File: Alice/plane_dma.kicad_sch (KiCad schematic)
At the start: 108 parts, among them Q647 NOT_OC, Q648 NOT_OC, Q649 NOT_OC, Q650 NOT_OC, Q651 NOT_OC, Q652 NOT_OC, Q653 NOT_OC, Q654 NOT_OC, Q655 NOT_OC, Q656 NOT_OC, Q657 NOT_OC, Q658 NOT_OC, Q659 NOT_OC, Q660 NOT_OC, Q661 NOT_OC, Q662 NOT_OC, Q663 NOT_OC, Q664 NOT_OC, Q665 NOT_OC, Q666 NOT_OC, Q667 NOT_OC, Q668 NOT_OC, Q669 NOT_OC, Q670 NOT_OC, Q671 NOT_OC, Q672 NOT_OC, Q673 NOT_OC, Q674 NOT_OC, Q675 NOT_OC, Q676 NOT_OC

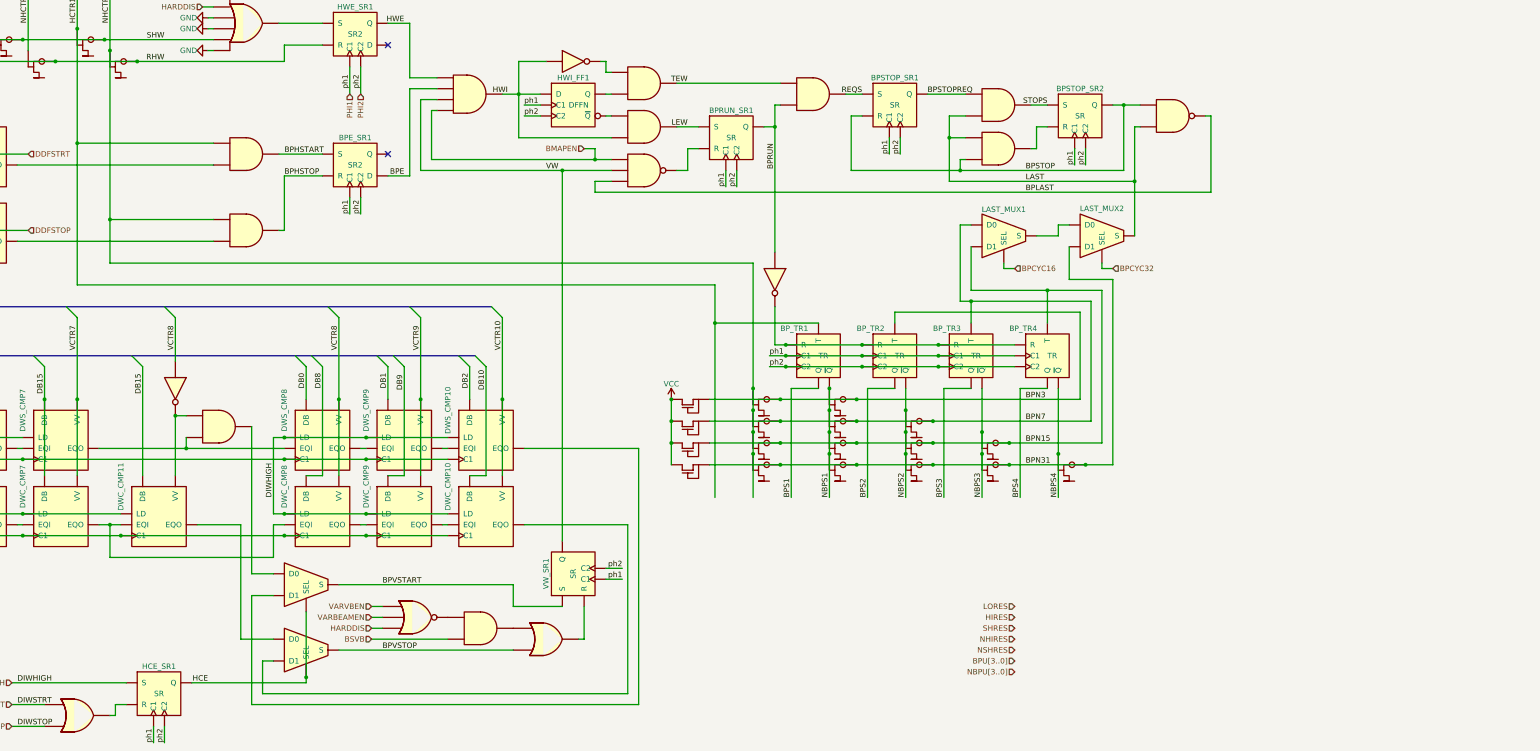
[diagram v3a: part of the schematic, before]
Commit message: Bitplane modulo logic added
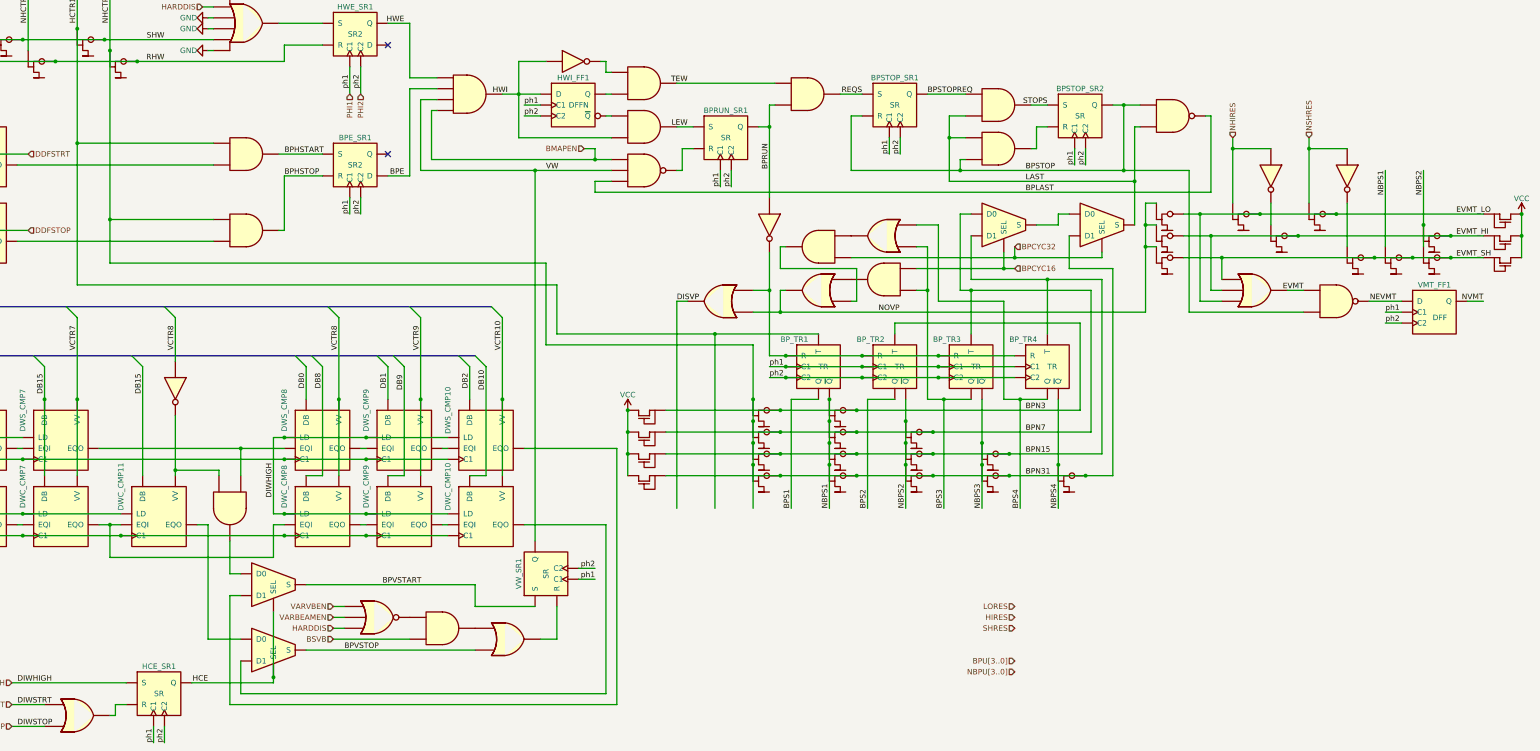
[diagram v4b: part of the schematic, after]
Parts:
- added AND_107, AND_108: AND2, symbol NMOS:AND2
- added NAND_8: NAND2, symbol NMOS:NAND2
- added NOT_33, NOT_34: NOT, symbol NMOS:NOT
- added OR_33, OR_34, OR_35: OR2, symbol NMOS:OR2
- added OR_36: OR3, symbol NMOS:OR3
- added Q685, Q686, Q687, Q688, Q689, Q690, Q691, Q692, Q693, Q694: NOT_OC, symbol NMOS:NOT_OC
- added R85, R86, R87: PULLUP, symbol NMOS:PULLUP
- added VMT_FF1: DFF, symbol NMOS:DFF
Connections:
- net BPCYC16: now also AND_108.3
- net BPCYC32: now also AND_107.2
- net BPS3: now also AND_108.2, OR_35.2
- net BPS4: now also OR_35.3
- net BPSTOP: now also NAND_8.3
- net NBPS1: now also Q692.2
- net NBPS2: now also Q693.2, Q694.2
- net NHIRES: now also NOT_33.2, Q688.2
- net NSHRES: now also NOT_34.2, Q690.2
- net PHI1: now also VMT_FF1.4 (C1)
- net PHI2: now also VMT_FF1.5 (C2)
- net VCC: now also R85.1 (S), R86.1 (S), R87.1 (S)
- net at BP_TR1.3 (R), BP_TR2.3 (R), BP_TR3.3 (R)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: now also OR_33.3
- net at DWC_CMP11.2 (VV), NOT_31.1: now also AND_94.3; no longer AND_94.2
- net at DWS_CMP7.6 (EQO), DWS_CMP8.5 (EQI): now also AND_94.2; no longer AND_94.3
- new net: NOT_34.1, Q691.2
- new net: NOT_33.1, Q689.2
- new net: AND_107.1, OR_34.2
- new net: AND_108.1, OR_34.3
- new net: AND_107.3, OR_35.1
- new net DISVP: OR_33.1
- new net EVMT: NAND_8.2, OR_36.1
- new net EVMT_HI: OR_36.3, Q686.1, Q689.1, Q693.1, R86.3 (D)
- new net EVMT_LO: OR_36.2, Q685.1, Q688.1, Q690.1, R85.3 (D)
- new net EVMT_SH: OR_36.4, Q687.1, Q691.1, Q692.1, Q694.1, R87.3 (D)
- new net NEVMT: NAND_8.1, VMT_FF1.3 (D)
- new net NOVP: OR_33.2, OR_34.1, Q685.2, Q686.2, Q687.2
- new net NVMT: VMT_FF1.1 (Q)
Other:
- moved on the sheet: BPRUN_SR1, BP_TR1, BP_TR2, BP_TR3, BP_TR4, VW_SR1

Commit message: Bitplane DMA runs in simulation
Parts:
- added AND_109: AND3, symbol NMOS:AND3
- added AND_110, AND_111, AND_112, AND_113, AND_114, AND_115, AND_116, AND_117, AND_118, AND_119, AND_120, AND_121, AND_122, AND_123, AND_124, AND_125, AND_126, AND_127: AND2, symbol NMOS:AND2
- added NOR_32, NOR_33: NOR2, symbol NMOS:NOR2
- added NOT_35: NOT, symbol NMOS:NOT
- added OR_37, OR_38, OR_39: OR6, symbol NMOS:OR6
- added OR_40: OR3, symbol NMOS:OR3
- added OR_41, OR_42, OR_43: OR2, symbol NMOS:OR2
- added Q695, Q696, Q697, Q698, Q699, Q700, Q701, Q702, Q703, Q704, Q705, Q706, Q707, Q708, Q709, Q710, Q711, Q712, Q713, Q714, Q715, Q716, Q717, Q718, Q719, Q720, Q721, Q722, Q723, Q724, Q725, Q726, Q727, Q728, Q729, Q730, Q731, Q732, Q733, Q734, Q735, Q736, Q737, Q738, Q739, Q740, Q741, Q742, Q743, Q744, Q745, Q746, Q747, Q748, Q749, Q750, Q751, Q752, Q753, Q754, Q755, Q756, Q757, Q758, Q759, Q760, Q761, Q762, Q763, Q764, Q765, Q766, Q767, Q768, Q769, Q770, Q771, Q772, Q773, Q774, Q775, Q776, Q777, Q778, Q779, Q780, Q781, Q782, Q783, Q784, Q785, Q786, Q787, Q788, Q789, Q790, Q791, Q792, Q793, Q794, Q795, Q796, Q797, Q798, Q799, Q800, Q801, Q802, Q803, Q804, Q805, Q806, Q807, Q808, Q809, Q810, Q811, Q812, Q813, Q814, Q815, Q816, Q817, Q818, Q819, Q820, Q821, Q822, Q823, Q824, Q825, Q826, Q827, Q828, Q829, Q830, Q831, Q832, Q833, Q834, Q835, Q836, Q837, Q838, Q839, Q840, Q841, Q842, Q843, Q844, Q845, Q846, Q847, Q848, Q849, Q850, Q851, Q852, Q853, Q854, Q855, Q856, Q857, Q858, Q859, Q860, Q861, Q862, Q863, Q864, Q865, Q866, Q867, Q868, Q869, Q870, Q871, Q872, Q873, Q874, Q875, Q876, Q877, Q878, Q879, Q880, Q881, Q882, Q883, Q884, Q885, Q886, Q887, Q888, Q889, Q890, Q891, Q892, Q893, Q894, Q895, Q896, Q897: NOT_OC, symbol NMOS:NOT_OC
- added R100, R101, R102, R103, R104, R105, R106, R107, R108, R88, R89, R90, R91, R92, R93, R94, R95, R96, R97, R98, R99: PULLUP, symbol NMOS:PULLUP
- added UVP_FF1, UVP_FF2, UVP_FF3, UVP_FF4, UVP_FF5, UVP_FF6, UVP_FF7, UVP_FF8: DFF, symbol NMOS:DFF
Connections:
- net BPS1: now also AND_114.2, AND_118.2, Q730.2, Q731.2, Q732.2, Q733.2, Q734.2, Q735.2
- net BPS2: now also AND_112.2, AND_119.2, AND_120.2, AND_124.2, AND_126.2, Q744.2, Q745.2
- net DISVP: now also Q695.2, Q696.2, Q697.2, Q698.2, Q699.2, Q700.2, Q701.2, Q702.2, Q703.2, Q704.2, Q705.2, Q706.2, Q707.2, Q708.2, Q709.2, Q710.2, Q711.2, Q712.2
- net GND: now also OR_38.5, OR_39.4
- net HCTR1: now also AND_113.2, Q713.2, Q714.2, Q715.2, Q716.2, Q717.2, Q718.2, Q719.2
- net NBPS1: now also AND_117.2, AND_121.2, Q736.2, Q737.2, Q738.2, Q739.2, Q740.2, Q741.2, Q742.2, Q743.2
- net NBPS2: now also AND_115.2, AND_122.2, AND_123.2, AND_125.2, AND_127.2, Q746.2, Q747.2, Q748.2, Q749.2
- net NHCTR1: now also AND_116.2, Q720.2, Q721.2, Q722.2, Q723.2, Q724.2, Q725.2, Q726.2, Q727.2, Q728.2, Q729.2
- net NHIRES: now also Q808.2, Q809.2, Q810.2, Q811.2, Q812.2, Q813.2, Q814.2, Q815.2, Q816.2, Q817.2, Q818.2, Q819.2, Q820.2, Q821.2, Q822.2, Q823.2
- net NSHRES: now also Q826.2, Q827.2, Q828.2, Q829.2, Q830.2, Q831.2, Q832.2, Q833.2, Q834.2, Q835.2, Q836.2
- net NVMT: now also NOR_32.3, NOR_33.2
- net PHI1: now also UVP_FF1.4 (C1), UVP_FF2.4 (C1), UVP_FF3.4 (C1), UVP_FF4.4 (C1), UVP_FF5.4 (C1), UVP_FF6.4 (C1), UVP_FF7.4 (C1), UVP_FF8.4 (C1)
- net PHI2: now also UVP_FF1.5 (C2), UVP_FF2.5 (C2), UVP_FF3.5 (C2), UVP_FF4.5 (C2), UVP_FF5.5 (C2), UVP_FF6.5 (C2), UVP_FF7.5 (C2), UVP_FF8.5 (C2)
- net VCC: now also R100.1 (S), R101.1 (S), R102.1 (S), R103.1 (S), R104.1 (S), R105.1 (S), R106.1 (S), R107.1 (S), R108.1 (S), R88.1 (S), R89.1 (S), R90.1 (S), R91.1 (S), R92.1 (S), R93.1 (S), R94.1 (S), R95.1 (S), R96.1 (S), R97.1 (S), R98.1 (S), R99.1 (S)
- net at NOT_34.1, Q691.2: now also Q837.2, Q838.2, Q839.2, Q840.2, Q841.2
- net at NOT_33.1, Q689.2: now also Q824.2, Q825.2
- new net: AND_125.1, OR_42.3
- new net: AND_117.1, OR_38.4
- new net: AND_122.1, OR_40.3
- new net: AND_114.1, OR_37.7
- new net: AND_124.1, OR_41.3
- new net: AND_126.1, OR_43.3
- new net: AND_115.1, OR_38.2
- new net: AND_119.1, OR_39.6
- new net: AND_112.1, OR_37.5
- new net: AND_121.1, OR_40.2
- new net: AND_118.1, OR_39.5
- new net: AND_120.1, OR_39.7
- new net: AND_113.1, OR_37.6
- new net: AND_123.1, OR_40.4
- new net: AND_116.1, OR_38.3
- new net BPU0: Q797.2, Q798.2, Q799.2, Q800.2, Q801.2, Q802.2, Q803.2
- new net BPU1: Q784.2, Q785.2, Q786.2, Q787.2, Q788.2, Q789.2, Q790.2
- new net BPU2: Q768.2, Q769.2, Q770.2, Q771.2, Q772.2, Q773.2, Q774.2, Q775.2, Q776.2, Q777.2
- new net BPU3: Q750.2, Q751.2, Q752.2, Q753.2, Q754.2, Q755.2, Q756.2, Q757.2, Q758.2, Q759.2, Q760.2, Q761.2, Q762.2, Q763.2
- new net DRB1: Q894.1, Q895.1, Q896.1, Q897.1
- new net DRB2: Q890.1, Q891.1, Q892.1, Q893.1
- new net DRB3: Q886.1, Q887.1, Q888.1, Q889.1
- new net DRB5: Q878.1, Q879.1, Q880.1, Q881.1, Q882.1, Q883.1, Q884.1, Q885.1
- new net DRB6: Q870.1, Q871.1, Q872.1, Q873.1, Q874.1, Q875.1, Q876.1, Q877.1
- new net DRB7: Q862.1, Q863.1, Q864.1, Q865.1, Q866.1, Q867.1, Q868.1, Q869.1
- new net EUVP: NOT_35.1
- new net EUVP1: OR_37.1, Q847.2, UVP_FF1.3 (D)
- new net EUVP12A: AND_112.3, AND_115.3, Q698.1, Q723.1, Q738.1, Q764.1, Q770.1, Q785.1, Q797.1, Q810.1, Q827.1, R91.3 (D)
- new net EUVP12B: AND_113.3, AND_116.3, Q699.1, Q753.1, Q771.1, Q791.1, Q798.1, Q825.1, R92.3 (D)
- new net EUVP12C: AND_114.3, AND_117.3, Q700.1, Q724.1, Q754.1, Q778.1, Q786.1, Q799.1, Q811.1, Q838.1, R93.3 (D)
- new net EUVP1A: OR_37.2, Q695.1, Q720.1, Q736.1, Q750.1, Q768.1, Q808.1, Q837.1, Q843.1, R88.3 (D)
- new net EUVP1B: OR_37.3, Q696.1, Q721.1, Q737.1, Q746.1, Q751.1, Q809.1, Q826.1, Q842.1, R89.3 (D)
- new net EUVP1C: OR_37.4, Q697.1, Q722.1, Q752.1, Q769.1, Q784.1, Q804.1, Q824.1, R90.3 (D)
- new net EUVP2: OR_38.1, Q848.2, UVP_FF2.3 (D)
- new net EUVP2A: OR_38.6, Q701.1, Q725.1, Q730.1, Q755.1, Q772.1, Q792.1, Q812.1, Q839.1, R94.3 (D)
- new net EUVP2B: OR_38.7, Q702.1, Q726.1, Q739.1, Q744.1, Q756.1, Q813.1, Q828.1, Q845.1, R95.3 (D)
- new net EUVP3: OR_39.1, Q849.2, UVP_FF3.3 (D)
- new net EUVP34A: AND_118.3, AND_121.3, Q705.1, Q714.1, Q759.1, Q779.1, Q787.1, Q800.1, Q816.1, Q841.1, R98.3 (D)
- new net EUVP34B: AND_119.3, AND_122.3, Q706.1, Q728.1, Q732.1, Q760.1, Q780.1, Q817.1, Q830.1, R99.3 (D)
- new net EUVP34C: AND_120.3, AND_123.3, Q707.1, Q729.1, Q733.1, Q765.1, Q775.1, Q788.1, Q801.1, Q818.1, Q831.1, R100.3 (D)
- new net EUVP3A: OR_39.2, Q703.1, Q727.1, Q731.1, Q747.1, Q757.1, Q773.1, Q793.1, Q805.1, Q814.1, Q829.1, R96.3 (D)
- new net EUVP3B: OR_39.3, Q704.1, Q713.1, Q740.1, Q758.1, Q774.1, Q794.1, Q806.1, Q815.1, Q840.1, R97.3 (D)
- new net EUVP4: OR_40.1, Q850.2, UVP_FF4.3 (D)
- new net EUVP5: OR_41.1, Q851.2, UVP_FF5.3 (D)
- new net EUVP56A: AND_124.3, AND_125.3, Q709.1, Q716.1, Q742.1, Q766.1, Q776.1, Q789.1, Q802.1, Q820.1, Q833.1, R102.3 (D)
- new net EUVP5A: OR_41.2, Q708.1, Q715.1, Q741.1, Q748.1, Q761.1, Q781.1, Q819.1, Q832.1, Q844.1, R101.3 (D)
- new net EUVP6: OR_42.1, Q852.2, UVP_FF6.3 (D)
- new net EUVP6A: OR_42.2, Q710.1, Q717.1, Q743.1, Q745.1, Q762.1, Q782.1, Q795.1, Q821.1, Q834.1, R103.3 (D)
- new net EUVP7: OR_43.1, Q846.2, UVP_FF7.3 (D)
- new net EUVP7A: OR_43.2, Q711.1, Q718.1, Q734.1, Q749.1, Q763.1, Q783.1, Q796.1, Q807.1, Q822.1, Q835.1, R104.3 (D)
- new net EUVP8: AND_127.1, Q853.2, UVP_FF8.3 (D)
- new net EUVP8A: AND_126.3, AND_127.3, Q712.1, Q719.1, Q735.1, Q767.1, Q777.1, Q790.1, Q803.1, Q823.1, Q836.1, R105.3 (D)
- new net NBPU0: AND_109.4, AND_110.3, Q804.2, Q805.2, Q806.2, Q807.2
- new net NBPU1: AND_109.3, AND_110.2, AND_111.3, Q791.2, Q792.2, Q793.2, Q794.2, Q795.2, Q796.2
- new net NBPU2: AND_109.2, AND_111.2, Q778.2, Q779.2, Q780.2, Q781.2, Q782.2, Q783.2
- new net NBPU3: Q764.2, Q765.2, Q766.2, Q767.2
- new net NBPU_01: AND_110.1, Q843.2, Q844.2
- new net NBPU_012: AND_109.1, Q842.2
- new net NBPU_12: AND_111.1, Q845.2
- new net NEUVP: NOT_35.2, Q846.1, Q847.1, Q848.1, Q849.1, Q850.1, Q851.1, Q852.1, Q853.1, R106.3 (D)
- new net NUVP_E: NOR_32.2, Q858.1, Q859.1, Q860.1, Q861.1, R108.3 (D)
- new net NUVP_O: NOR_33.3, Q854.1, Q855.1, Q856.1, Q857.1, R107.3 (D)
- new net UVM1: NOR_33.1
- new net UVM2: NOR_32.1
- new net UVP1: Q854.2, Q862.2, Q870.2, Q878.2, Q886.2, Q890.2, Q894.2, UVP_FF1.1 (Q)
- new net UVP2: Q858.2, Q863.2, Q871.2, Q879.2, Q887.2, Q891.2, UVP_FF2.1 (Q)
- new net UVP3: Q855.2, Q864.2, Q872.2, Q880.2, Q888.2, Q895.2, UVP_FF3.1 (Q)
- new net UVP4: Q859.2, Q865.2, Q873.2, Q881.2, Q889.2, UVP_FF4.1 (Q)
- new net UVP5: Q856.2, Q866.2, Q874.2, Q882.2, Q892.2, Q896.2, UVP_FF5.1 (Q)
- new net UVP6: Q860.2, Q867.2, Q875.2, Q883.2, Q893.2, UVP_FF6.1 (Q)
- new net UVP7: Q857.2, Q868.2, Q876.2, Q884.2, Q897.2, UVP_FF7.1 (Q)
- new net UVP8: Q861.2, Q869.2, Q877.2, Q885.2, UVP_FF8.1 (Q)
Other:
- note added: "$110"
- note added: "$112"
- note added: "$114"
- note added: "$116"
- note added: "$118"
- note added: "$11A"
- note added: "$11C"
- note added: "$11E"

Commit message: Schematics have been annotated
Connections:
- net NNSHRES: now reaches NOT_34.1, Q691.2, Q837.2, Q838.2, Q839.2, Q840.2, Q841.2
- net NNHIRES: now reaches NOT_33.1, Q689.2, Q824.2, Q825.2
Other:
- note added: "Bitplane RUN logic"
- note added: "DIWHIGH logic"
- note added: "Display Data Fetch sequencer PLA"
- note added: "Early Use Video Pointer"
- note added: "Hardware window"
- note added: "Modulo add pulse"
- note added: "Use Video Modulo #1 (Odd)"
- note added: "Use Video Modulo #2 (Even)"
- note added: "Use Video Pointer #1"
- note added: "Use Video Pointer #2"
- note added: "Use Video Pointer #3"
- note added: "Use Video Pointer #4"
- note added: "Use Video Pointer #5"
- note added: "Use Video Pointer #6"
- note added: "Use Video Pointer #7"
- note added: "Use Video Pointer #8"
- moved on the sheet: HCE_SR1, UVP_FF1, UVP_FF2, UVP_FF3, UVP_FF4, UVP_FF5, UVP_FF6, UVP_FF7, UVP_FF8

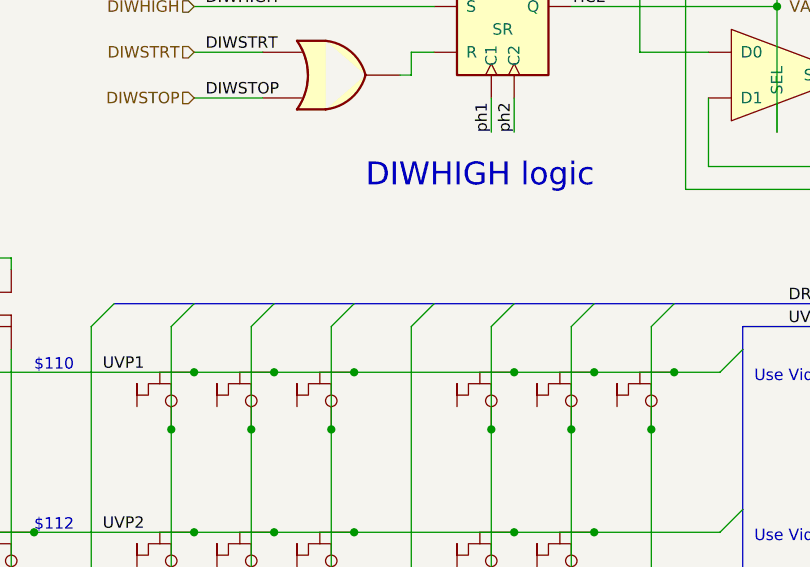
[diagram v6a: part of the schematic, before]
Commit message: Added Copper DMA schematics (WIP)
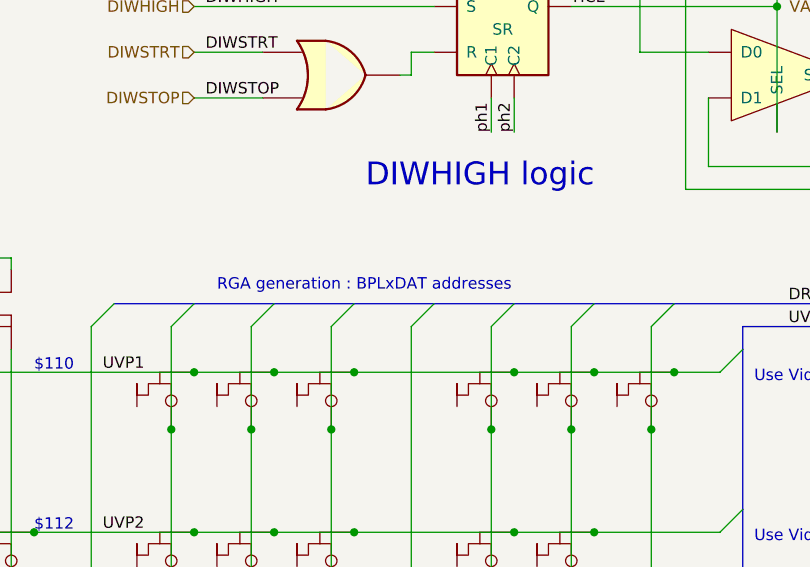
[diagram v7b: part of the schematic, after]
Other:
- note added: "RGA generation : BPLxDAT addresses"
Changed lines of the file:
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@@
     (stroke (width 0) (type default) (color 0 0 0 0))
   )
-  (bus_entry (at 224.79 251.46) (size 2.54 -2.54)
+  (bus_entry (at 224.79 269.24) (size 2.54 -2.54)
     (stroke (width 0) (type default) (color 0 0 0 0))
   )
-  (bus_entry (at 224.79 233.68) (size 2.54 -2.54)
+  (bus_entry (at 224.79 287.02) (size 2.54 -2.54)
     (stroke (width 0) (type default) (color 0 0 0 0))
   )
@@
     (stroke (width 0) (type default) (color 0 0 0 0))
   )
-  (bus_entry (at 224.79 269.24) (size 2.54 -2.54)
+  (bus_entry (at 224.79 251.46) (size 2.54 -2.54)
     (stroke (width 0) (type default) (color 0 0 0 0))
   )
-  (bus_entry (at 224.79 287.02) (size 2.54 -2.54)
+  (bus_entry (at 224.79 233.68) (size 2.54 -2.54)
     (stroke (width 0) (type default) (color 0 0 0 0))
   )
@@
     (stroke (width 0) (type default) (color 0 0 0 0))
   )
-  (bus_entry (at 422.91 151.13) (size 2.54 -2.54)
+  (bus_entry (at 440.69 151.13) (size 2.54 -2.54)
     (stroke (width 0) (type default) (color 0 0 0 0))
   )
-  (bus_entry (at 414.02 156.21) (size 2.54 -2.54)
+  (bus_entry (at 458.47 151.13) (size 2.54 -2.54)
     (stroke (width 0) (type default) (color 0 0 0 0))
   )
-  (bus_entry (at 431.8 156.21) (size 2.54 -2.54)
+  (bus_entry (at 422.91 151.13) (size 2.54 -2.54)
     (stroke (width 0) (type default) (color 0 0 0 0))
   )
-  (bus_entry (at 440.69 151.13) (size 2.54 -2.54)
+  (bus_entry (at 414.02 156.21) (size 2.54 -2.54)
     (stroke (width 0) (type default) (color 0 0 0 0))
   )
-  (bus_entry (at 458.47 151.13) (size 2.54 -2.54)
+  (bus_entry (at 431.8 156.21) (size 2.54 -2.54)
     (stroke (width 0) (type default) (color 0 0 0 0))
   )
@@
     (effects (font (size 1.27 1.27)) (justify left bottom))
   )
+  (text "RGA generation : BPLxDAT addresses" (at 168.91 207.01 0)
+    (effects (font (size 1.27 1.27)) (justify left bottom))
+  )
